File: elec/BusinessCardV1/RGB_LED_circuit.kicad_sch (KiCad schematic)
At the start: 35 parts, among them Q3 DMG2305UX-7, Q4 DMG2305UX-7, Q5 DMG2305UX-7, Q6 DMG1012UW-7, Q7 DMG1012UW-7, Q8 DMG1012UW-7, U15 TC4069UBFTEL_N, U16 SN74LVC1G139DCTR, U17 SN74LV161ADR, U20 TLC555CDR

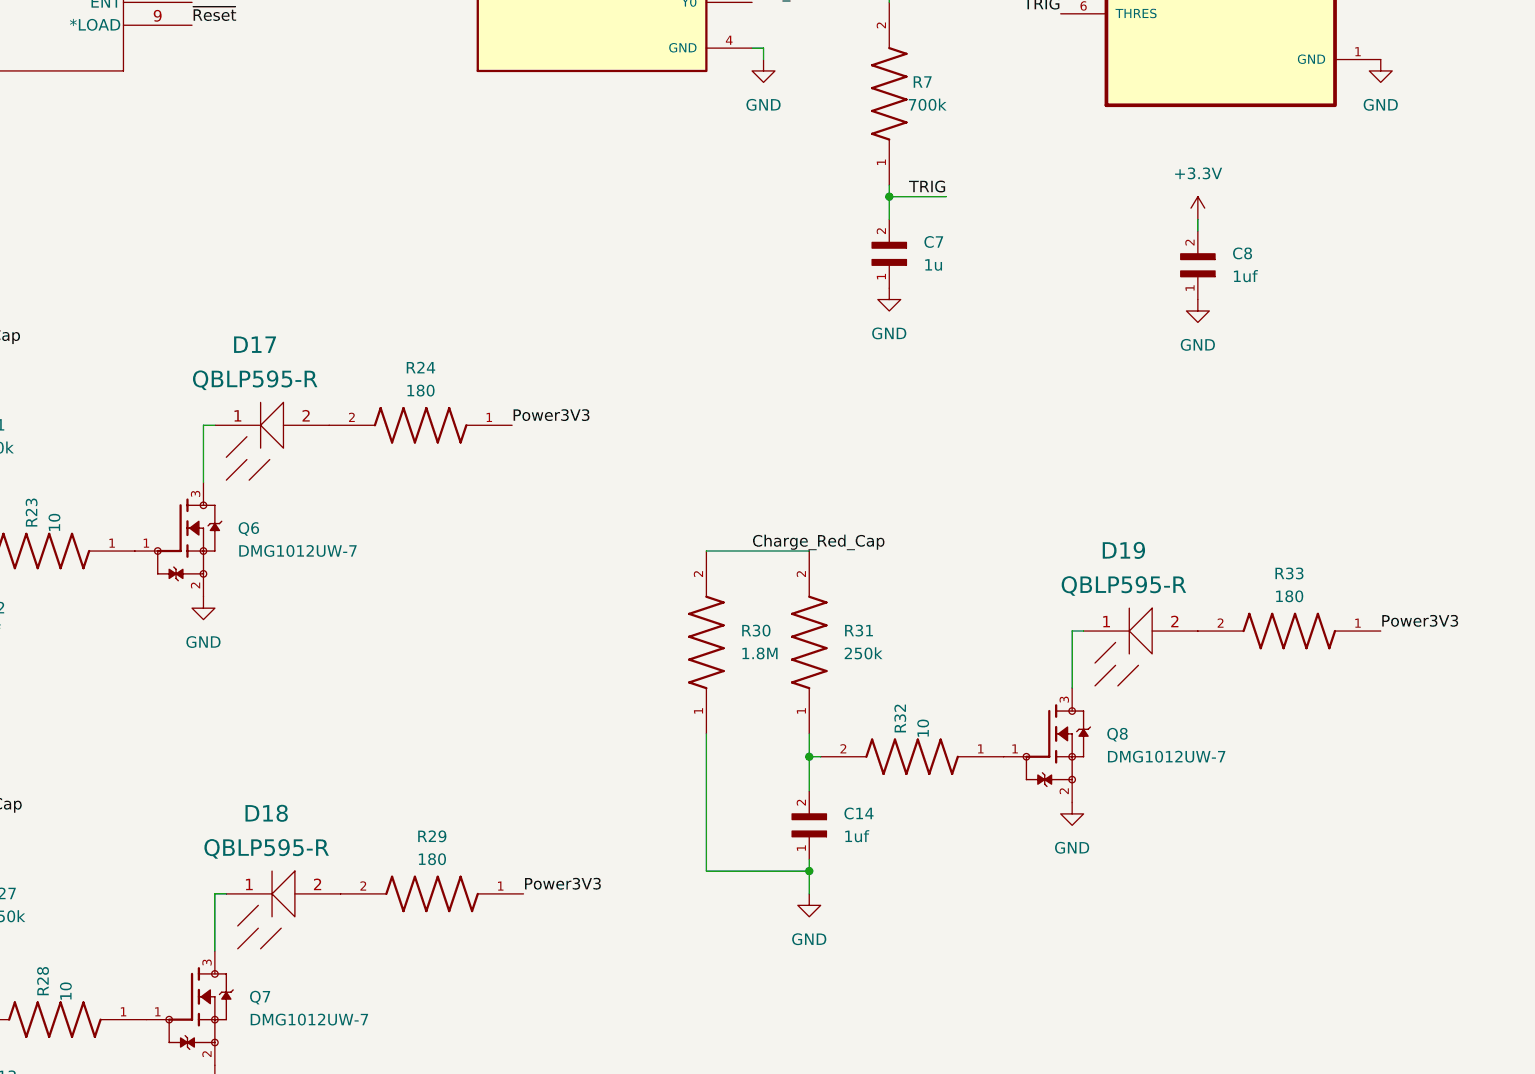
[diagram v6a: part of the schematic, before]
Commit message: Started layout
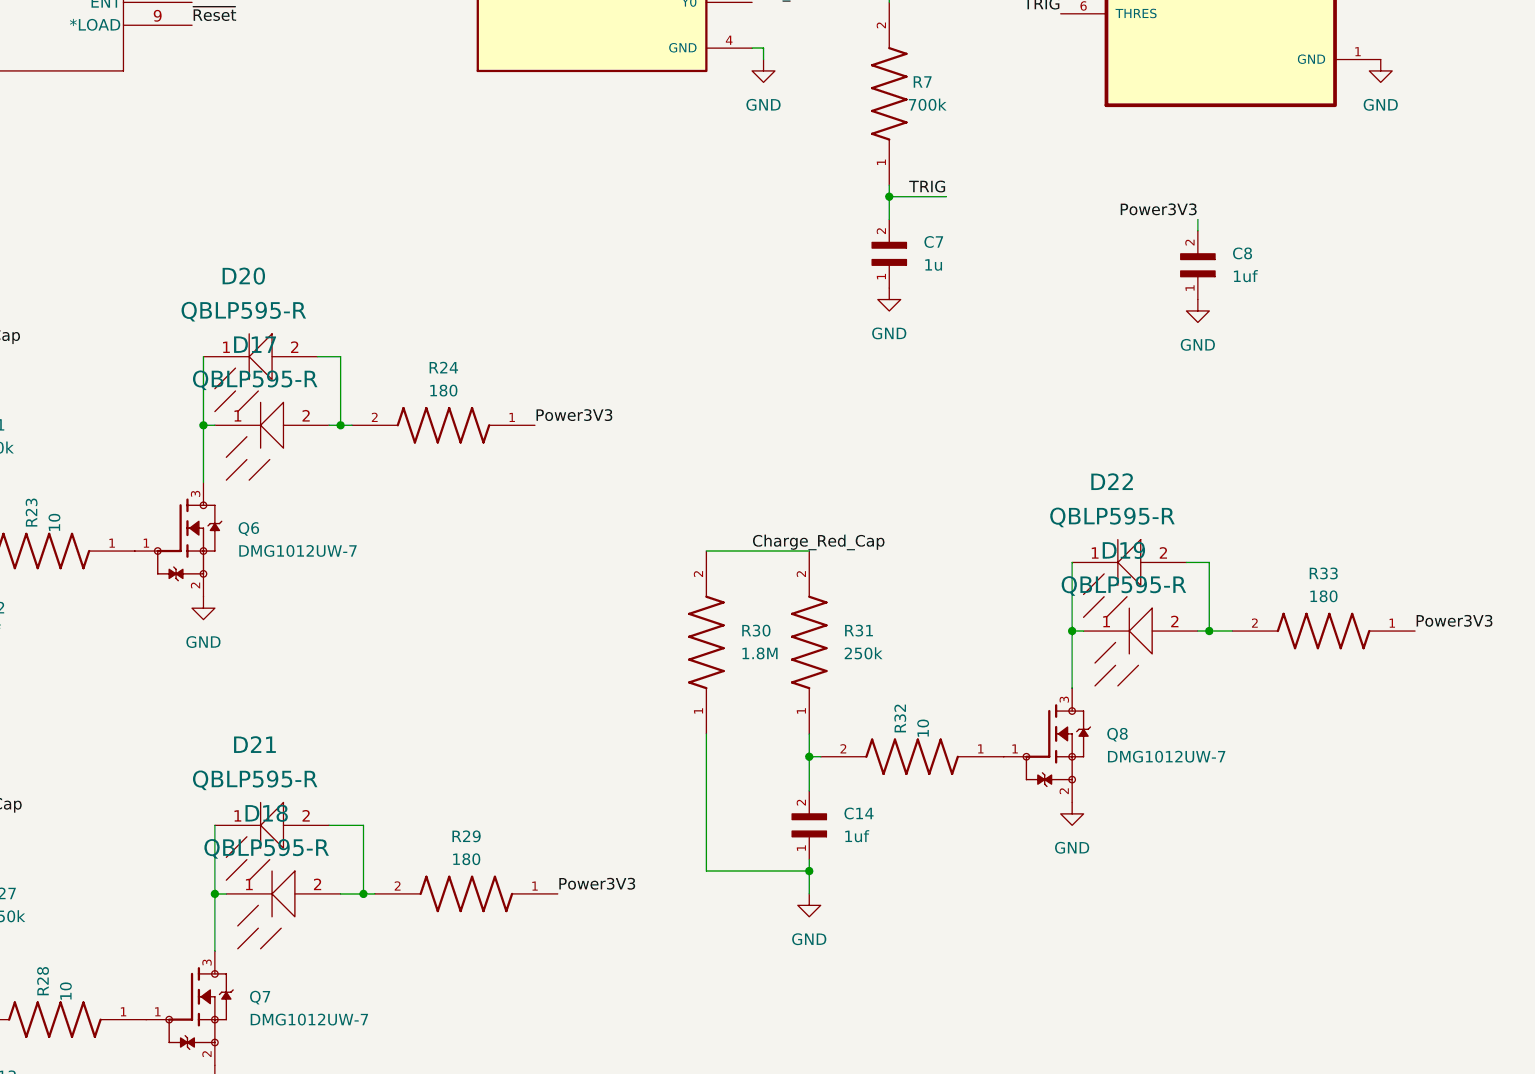
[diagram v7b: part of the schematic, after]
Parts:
- added D20, D21, D22: QBLP595-R, LED_SMD:LED_0402_1005Metric_Pad0.77x0.64mm_HandSolder, symbol QBLP595:QTB-LED-0002
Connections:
- net +3.3V is gone; now on net Power3V3: C8.2
- net at D17.1 (CATHODE_(-)), Q6.3: now also D20.1 (CATHODE_(-))
- net at D17.2 (ANODE_(+)), R24.2: now also D20.2 (ANODE_(+))
- net at D19.1 (CATHODE_(-)), Q8.3: now also D22.1 (CATHODE_(-))
- net at D19.2 (ANODE_(+)), R33.2: now also D22.2 (ANODE_(+))
- net at D18.1 (CATHODE_(-)), Q7.3: now also D21.1 (CATHODE_(-))
- net at D18.2 (ANODE_(+)), R29.2: now also D21.2 (ANODE_(+))
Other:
- moved on the sheet: R24, R29, R33

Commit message: Push before destroying everything
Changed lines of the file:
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@@
+		)
+	)
+	(global_label "Power3V3"
+		(shape input)
+		(at 279.4 33.02 0)
+		(fields_autoplaced yes)
+		(effects
+			(font
+				(size 1.27 1.27)
+			)
+			(justify left)
+		)
+		(property "Intersheetrefs" "${INTERSHEET_REFS}"
+			(at 291.5171 33.02 0)
+			(effects
+				(font
+					(size 1.27 1.27)
+				)
+				(justify left)
+				(hide yes)
+			)
 		)
 	)
